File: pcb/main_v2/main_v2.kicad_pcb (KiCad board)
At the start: 4 copper layers, 98 x 176.2 mm, 95 parts, among them IC201 AP22811AW5-7, IC301 SE2576L-R, IC302 RMS-30+, IC401 RMS-30+, IC402 HMC374, IC501 SPF5043Z, IC502 PD0922J5050S2HF, IC503 SPF5043Z, J101 Conn_02x08_Top_Bottom, J201 USB_A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

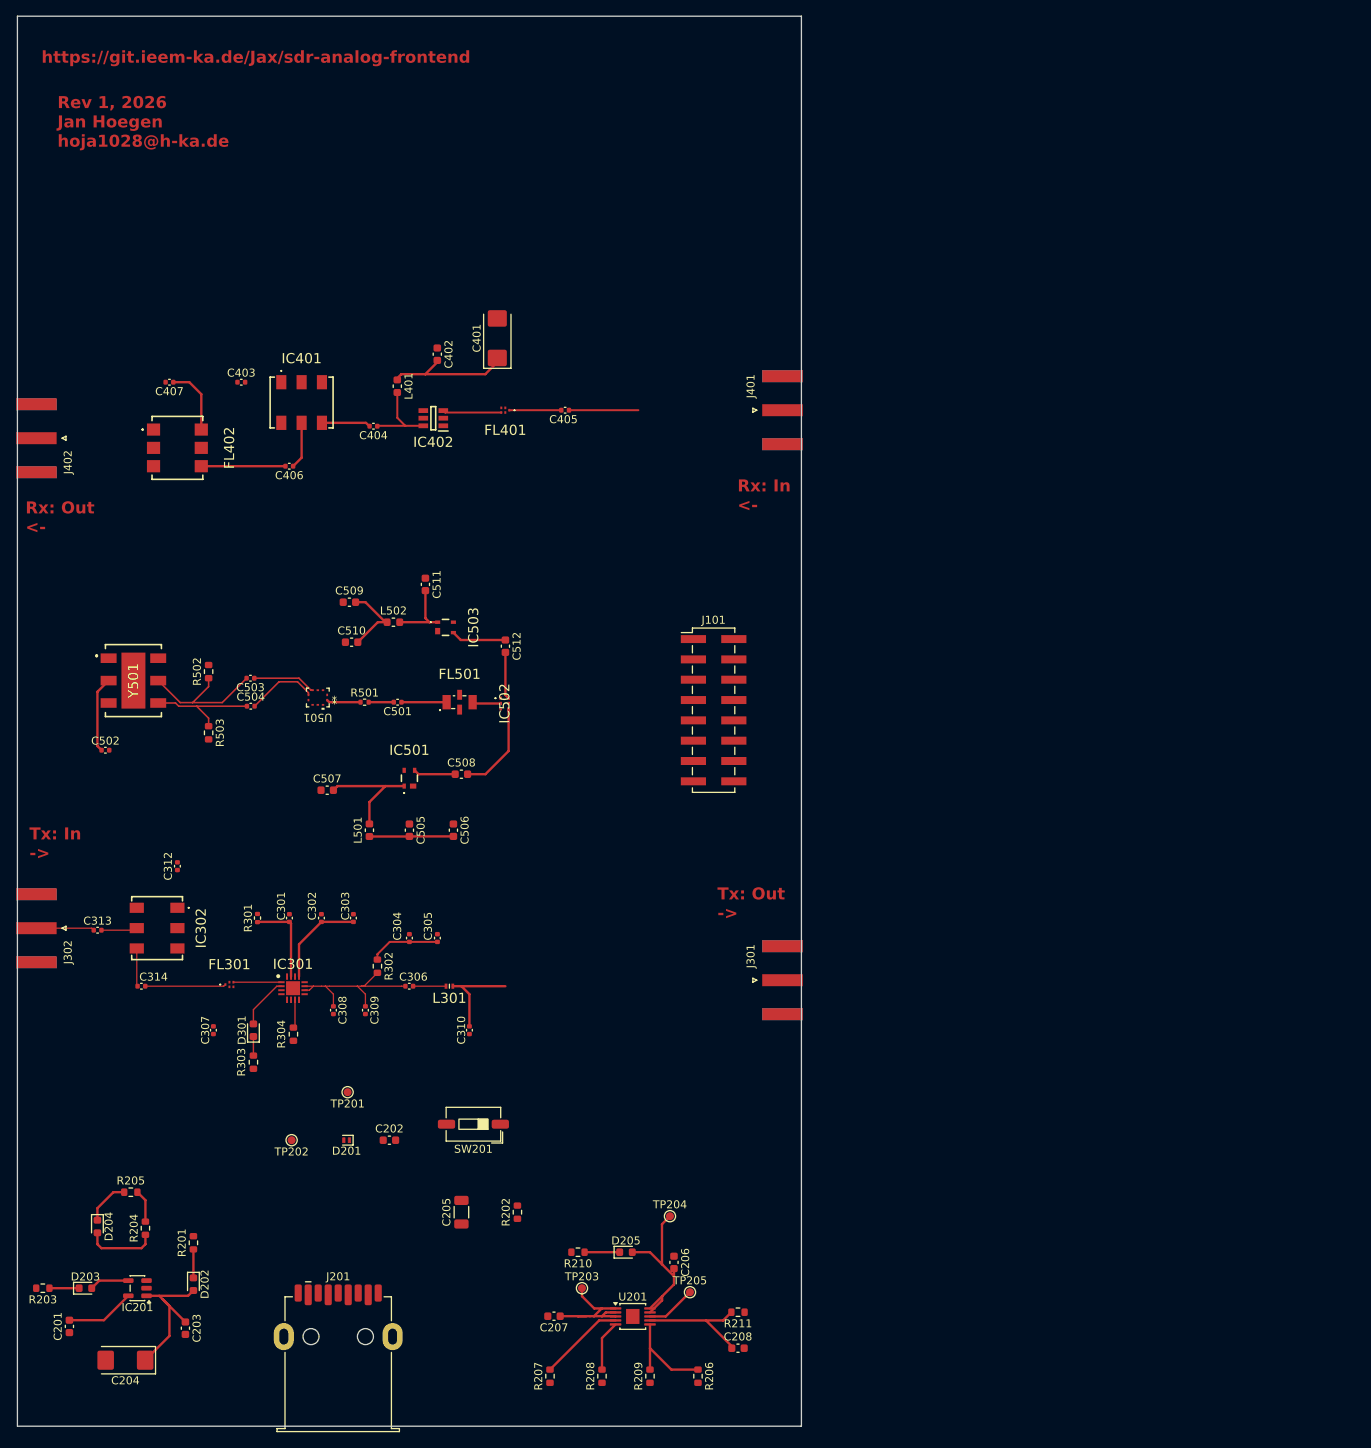
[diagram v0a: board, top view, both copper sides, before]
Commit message: updated layout
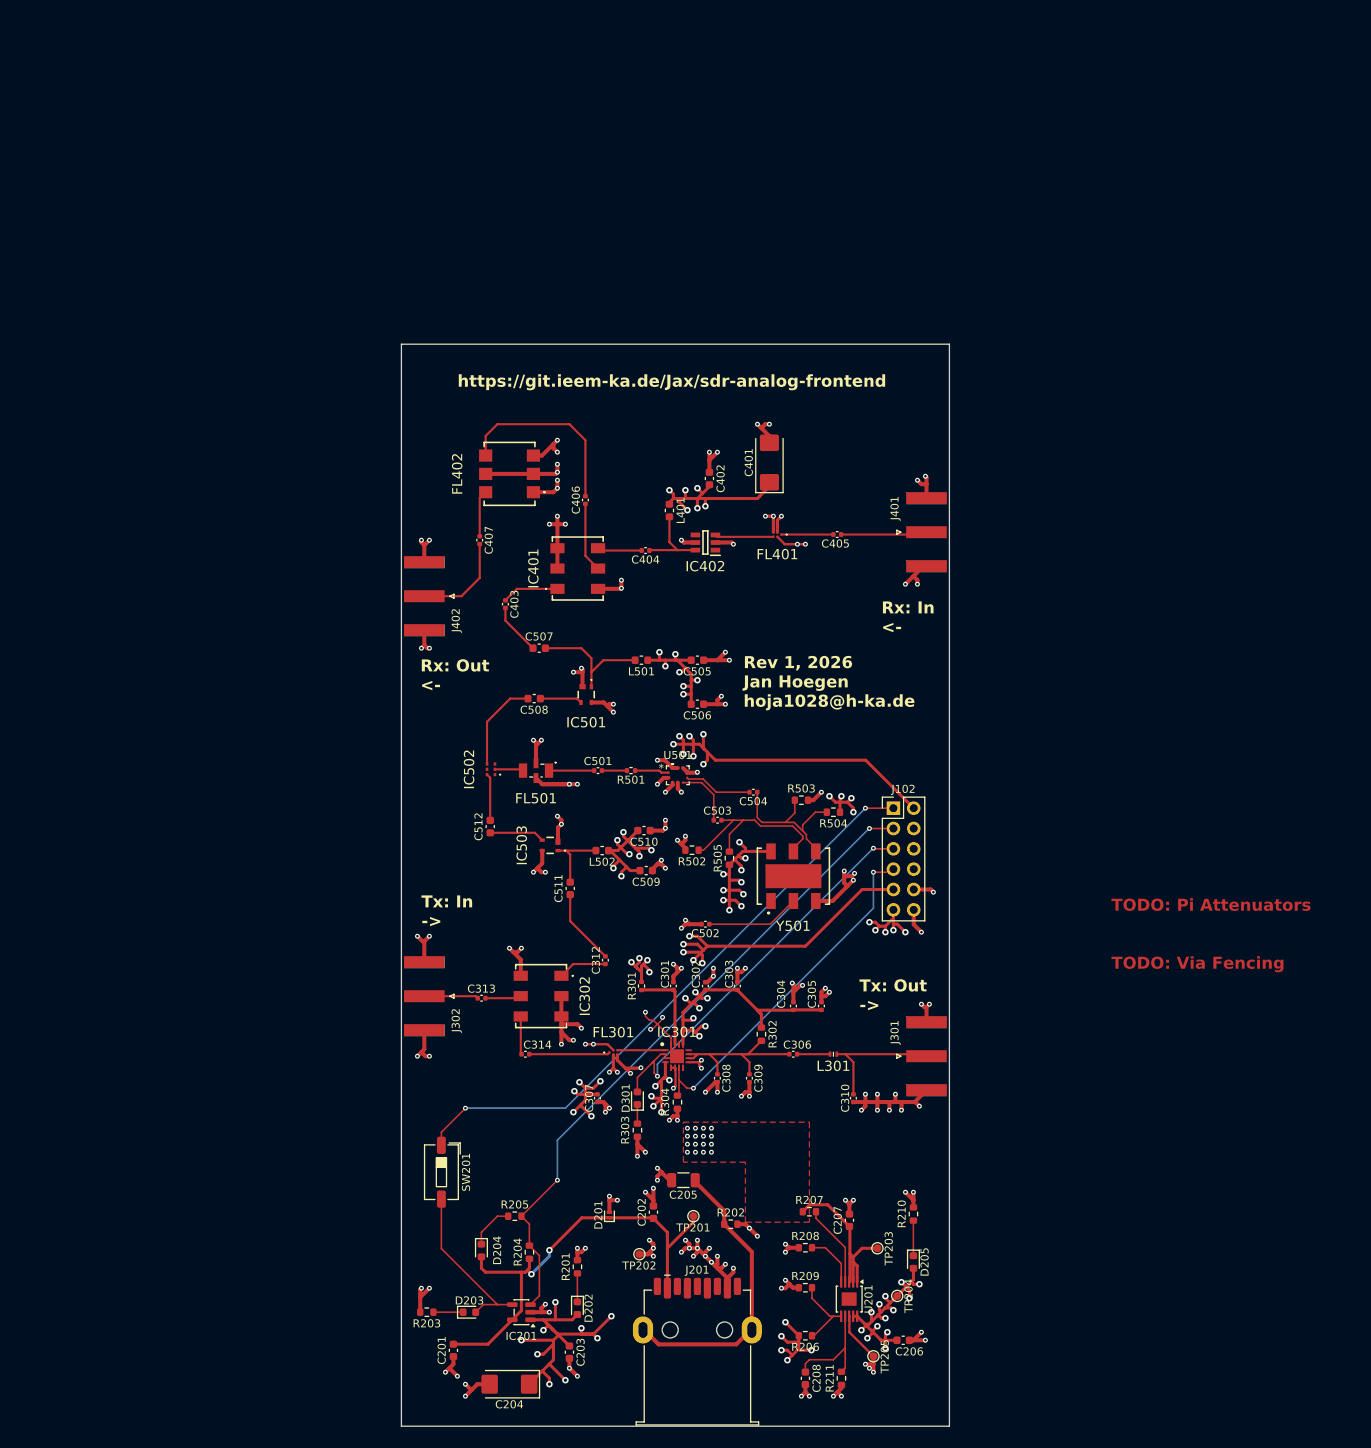
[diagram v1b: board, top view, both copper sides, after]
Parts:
- removed J101: Conn_02x08_Top_Bottom, Connector_PinHeader_2.54mm:PinHeader_2x08_P2.54mm_Vertical_SMD
- added J102: Conn_02x06_Odd_Even, Connector_PinHeader_2.54mm:PinHeader_2x06_P2.54mm_Vertical, F.Cu at (135.0, 115.0)
- added R504: DNI, Resistor_SMD:R_0603_1608Metric, F.Cu at (127.5, 115.5)
- added R505: DNI, Resistor_SMD:R_0603_1608Metric, F.Cu at (114.5, 121.2)
- moved Y501 86.0 mm to (122.5, 123.5), turned to 0 degrees
- moved C502 78.1 mm to (111.5, 129.5), turned to 180 degrees
- moved R503 74.6 mm to (123.5, 114.0), turned to 0 degrees
- moved R502 64.4 mm to (109.8, 120.2), turned to 180 degrees
- moved C504 63.7 mm to (117.5, 113.0), turned to 180 degrees
- moved C503 61.0 mm to (113.0, 116.5), turned to 0 degrees
- moved C312 54.8 mm to (99.0, 134.0)
- moved J402 52.4 mm to (76.4, 88.5)
- moved C509 50.0 mm to (104.1, 122.8), turned to 180 degrees
- moved J302 49.2 mm to (76.4, 138.5)
- moved R301 48.7 mm to (103.5, 137.2)
- moved C301 48.7 mm to (107.5, 137.2)
- moved C302 48.7 mm to (111.5, 137.2)
- moved C303 48.7 mm to (115.5, 137.2)
- moved C304 48.7 mm to (122.5, 139.7)
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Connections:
- net Net-(J201-Shield) renamed /power/Shield
- C507 pad 1: Carrier Frequency: Tx -> Carrier Frequency: Rx
- C511 pad 1: Carrier Frequency: Rx -> Carrier Frequency: Tx
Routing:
- net GND: track 6.26 -> 342.7 mm, vias 0 -> 168
- net +5V: track 95.4 -> 279.6 mm, vias 0 -> 78
- net CONN-2: track 4.09 -> 81.9 mm, vias 0 -> 2
- net CONN-1: track 0.00 -> 74.9 mm, vias 0 -> 2
- net +3.3V: track 21.7 -> 81.9 mm, vias 0 -> 37
- net CONN-3: track 6.50 -> 51.2 mm, vias 0 -> 2
- net USB Power: track 17.6 -> 59.0 mm, vias 0 -> 2
- net CONN-4: track 3.56 -> 44.7 mm, vias 0 -> 2
- net /power/Shield: track 0.00 -> 37.8 mm
- net Net-(D203-A): track 4.97 -> 21.1 mm
- net /receiver/downconverted Rx 1: track 10.5 -> 23.4 mm
- net /receiver/low filtered Rx 1: track 0.00 -> 12.6 mm
- net Carrier Frequency: Tx: track 0.00 -> 9.54 mm
- net /receiver/lo in: track 0.00 -> 7.10 mm
- net /oscillator/TCX P: track 17.3 -> 23.9 mm
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- added copper zone on In2.Cu, net +3.3V
- added copper zone on F.Cu, net +5V
- added copper zone on In2.Cu, net +5V
- added copper zone on In1.Cu, net GND
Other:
- board size 98 x 176.2 mm -> 68.5 x 135.2 mm
- board text added: "TODO: Pi Attenuators"
- board text added: "TODO: Via Fencing"
- board text added: "{ "ViaStitching": "0.2", "stitch_zone_0": { "HSpacing": "40", "VSpacing": "40", "HOffset": "0", "VOffset": "0", "Clearance": "0", "Randomize": false }, "stitch_zone_1": { "HSpacing": "100", "VSpacing": "100", "HOffset": "0", "VOffset": "0", "Clearance": "0", "Randomize": false } }"

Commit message: update layout
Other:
- board text removed: "TODO: Pi Attenuators"
- board text removed: "TODO: Via Fencing"
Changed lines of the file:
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@@
 		(capping no)
 		(filling no)
-		(zone_defaults)
 		(pcbplotparams
 			(layerselection 0x00000000_00000000_55555555_57555501)
@@
 		(layer "Edge.Cuts")
 	)
-	(gr_text "TODO: Pi Attenuators"
-		(at 162.25 128 0)
-		(layer "F.Cu")
-		(effects
-			(font
-				(size 1.5 1.5)
-				(thickness 0.3)
-				(bold yes)
-			)
-			(justify left bottom)
-		)
-	)
-	(gr_text "TODO: Via Fencing"
-		(at 162.25 135.25 0)
-		(layer "F.Cu")
-		(effects
-			(font
-				(size 1.5 1.5)
-				(thickness 0.3)
-				(bold yes)
-			)
-			(justify left bottom)
-		)
-	)
 	(gr_text "Rx: Out\n<-"
